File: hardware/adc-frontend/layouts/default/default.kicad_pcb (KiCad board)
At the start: 4 copper layers, 142.2 x 111.6 mm, 135 parts

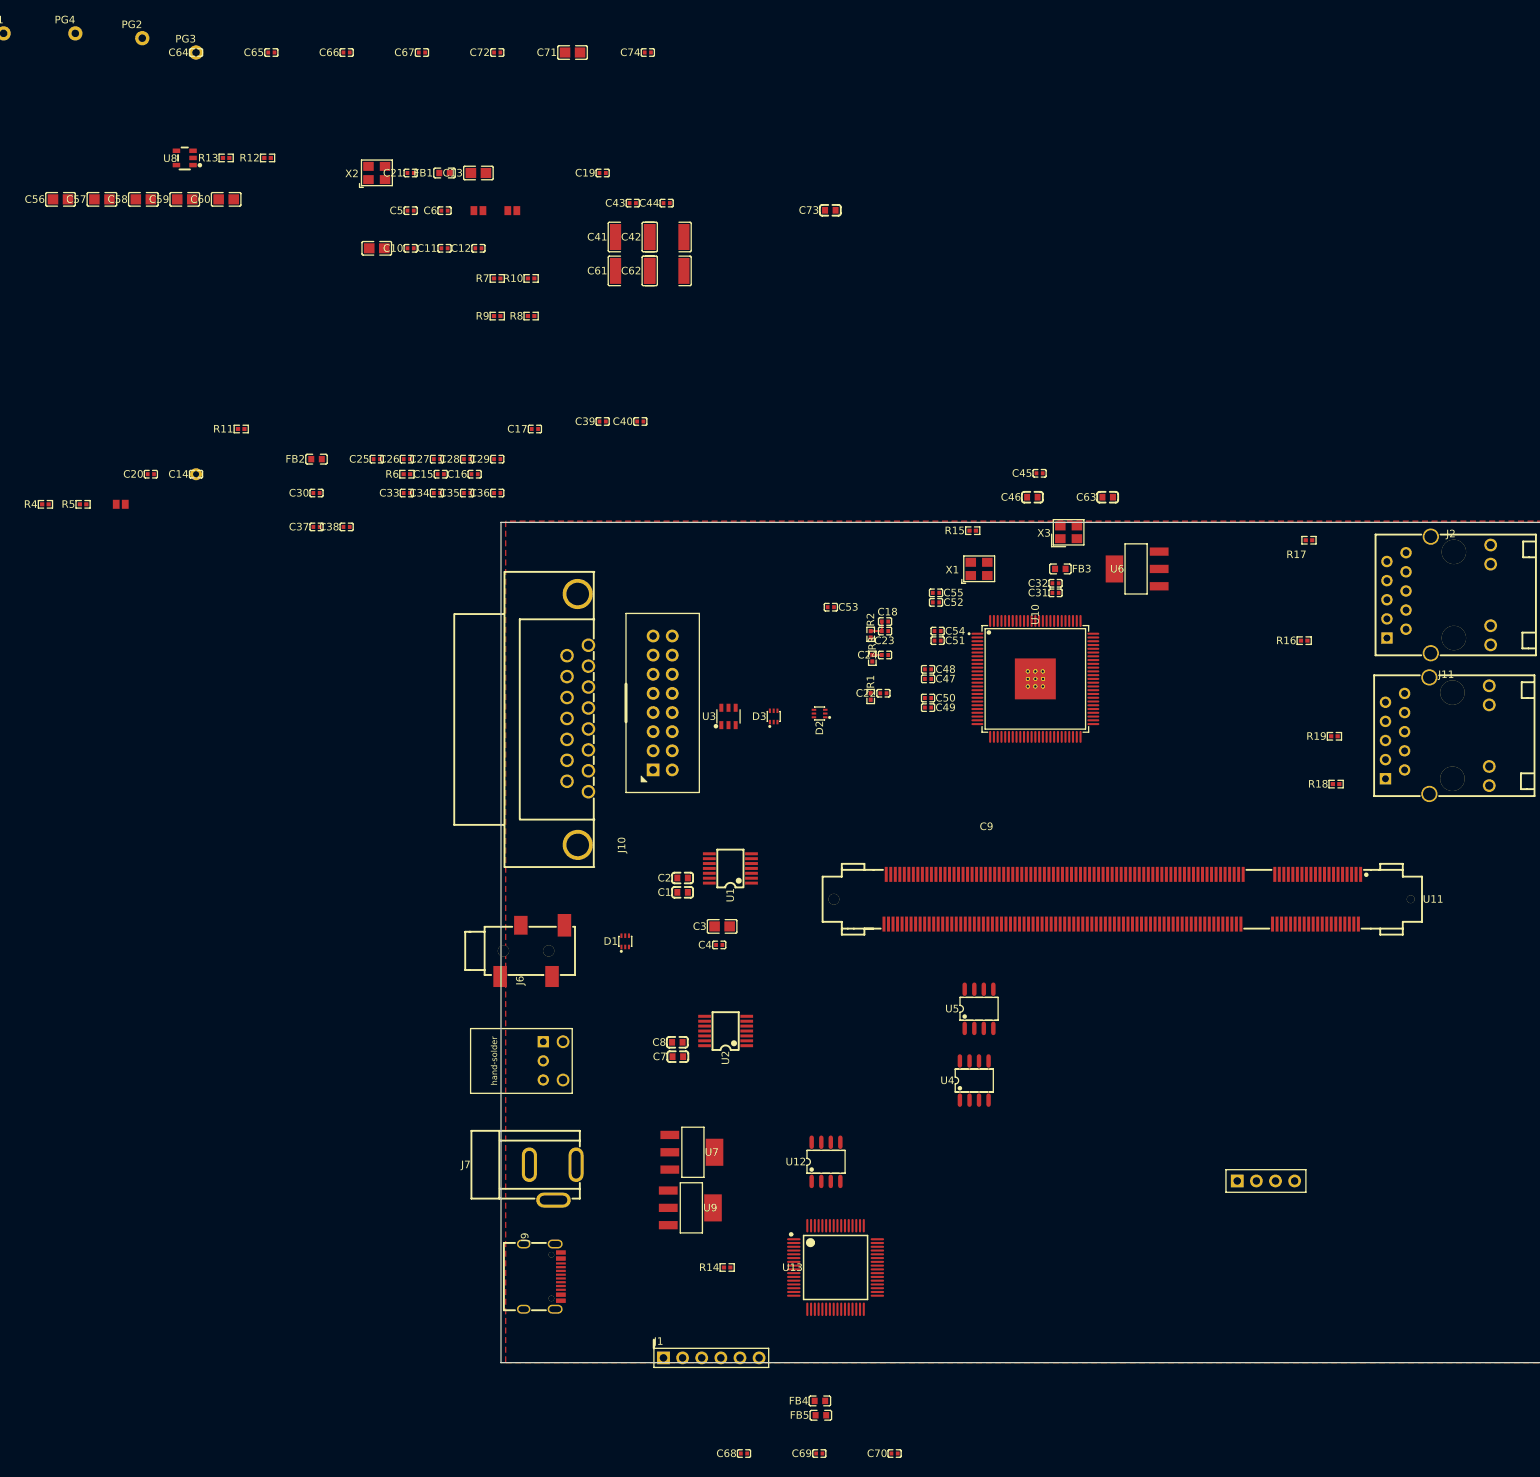
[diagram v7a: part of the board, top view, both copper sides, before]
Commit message: passives: 各パッシブに値をassertで付与しKiCad Value表示を修正
`{ℝ+}F`/`{ℝ+}Ω` の文字化けを解消。原因はatomic part(by_supplier)が
電気値属性を持たず、has_simple_value_representationが未拘束パラメータを
表示していたため。`param = 値`はsuperset化されず表示に反映されないので、
`assert resistance/capacitance within lo to hi` で拘束(R=±1%, C=±5〜10%)。
→ KiCadのValueが 75Ω ±1% / 4.7nF ±10% 等に。max_power/max_voltageは
隠しプロパティのため未拘束のまま(表示・配線に影響なし)。

Co-Authored-By: Claude Opus 4.8 (1M context) <noreply@anthropic.com>
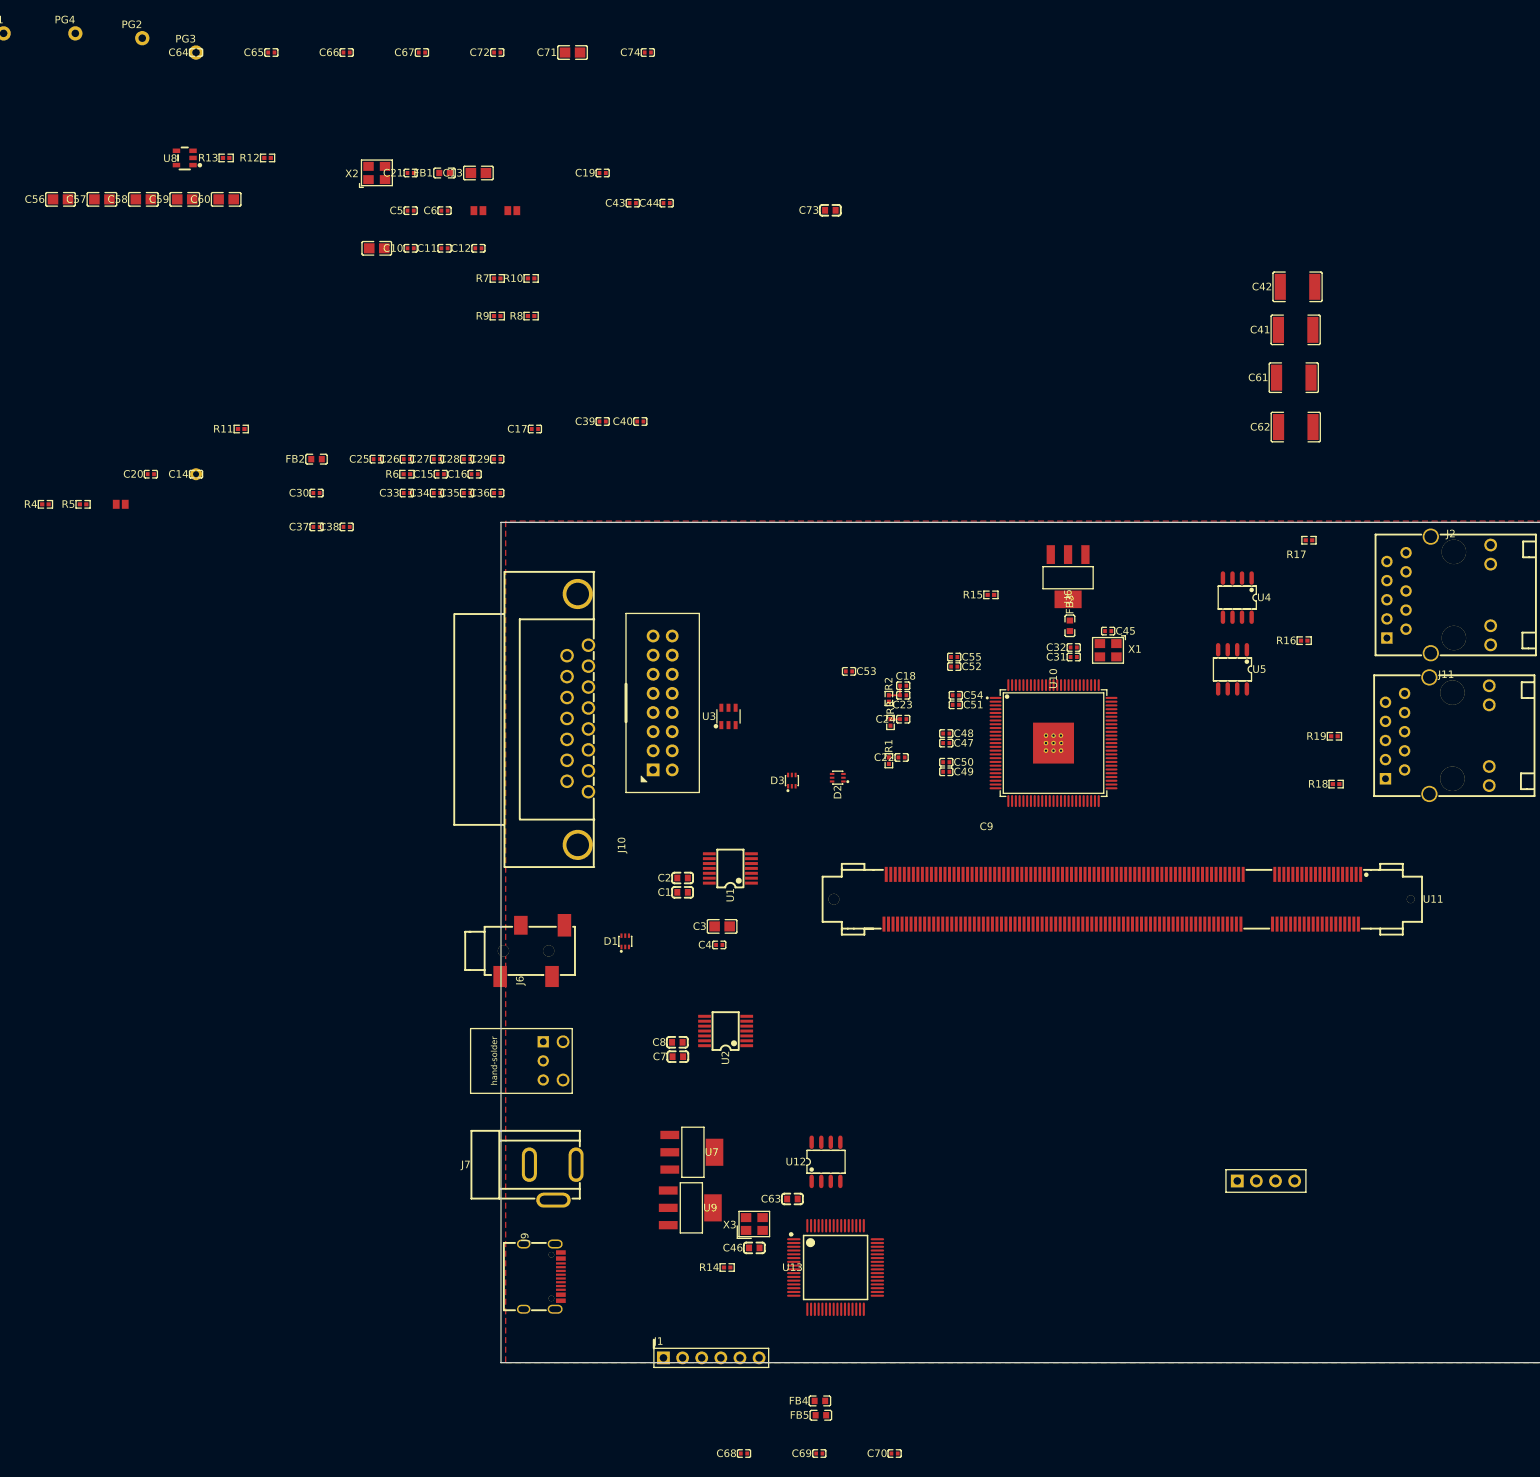
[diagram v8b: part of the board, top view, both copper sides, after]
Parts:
- C1, C2, C7, C73, C8: value {ℝ+}F -> 1µF ±10%
- C10, C11, C12, C14, C15, C17, C19, C21, C22, C23, C24, C25, C26, C27, C28, C29, C30, C31, C32, C33, C34, C35, C36, C37, C38, C39, C4, C40, C43, C44, C45, C5, C6, C64, C65, C66, C67, C68, C69, C70, C72, C74: value {ℝ+}F -> 100nF ±10%
- C13, C3, C56, C57, C58, C59, C60, C71, C9: value {ℝ+}F -> 10µF ±10%
- C16, C41, C42, C61, C62: value {ℝ+}F -> 4.7nF ±10%
- C18, C20, C54, C55: value {ℝ+}F -> 1nF ±10%
- C46, C63: value {ℝ+}F -> 33pF ±5%
- C47, C48, C49, C50, C51, C52, C53: value {ℝ+}F -> 10nF ±10%
- R1, R2, R3: value {ℝ+}Ω -> 75Ω ±1%
- R10, R7, R8, R9: value {ℝ+}Ω -> 2.2kΩ ±1%
- R11, R16, R17, R18, R19: value {ℝ+}Ω -> 220Ω ±1%
- R12: value {ℝ+}Ω -> 62Ω ±1%
- R13: value {ℝ+}Ω -> 120Ω ±1%
- R14: value {ℝ+}Ω -> 12kΩ ±1%
- R15: value {ℝ+}Ω -> 10kΩ ±1%
- R4, R5: value {ℝ+}Ω -> 5.1kΩ ±1%
- R6: value {ℝ+}Ω -> 1.5kΩ ±1%
- moved C46 106.3 mm to (104.1, 158.8)
- moved C63 102.2 mm to (109.2, 152.2)
- moved X3 100.9 mm to (104.1, 155.6)
- moved C61 88.9 mm to (175.8, 43.2)
- moved C41 88.9 mm to (176.0, 36.8)
- moved C62 86.1 mm to (176.0, 49.7)
- moved C42 84.0 mm to (176.3, 31.1)
- moved U4 73.0 mm to (168.3, 72.4), turned to 180 degrees
- moved U5 56.3 mm to (167.6, 81.9), turned to 180 degrees
- moved C45 22.8 mm to (151.1, 76.8), turned to 180 degrees
- moved X1 20.3 mm to (151.1, 79.4), turned to 180 degrees
- moved U6 9.19 mm to (145.8, 69.6), turned to 90 degrees
- moved C18 8.86 mm to (123.9, 84.1)
- moved C23 8.86 mm to (123.9, 85.4)
- moved C53 8.86 mm to (116.7, 82.2)
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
